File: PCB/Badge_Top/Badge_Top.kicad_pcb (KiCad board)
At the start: 2 copper layers, 65 x 75 mm, 34 parts

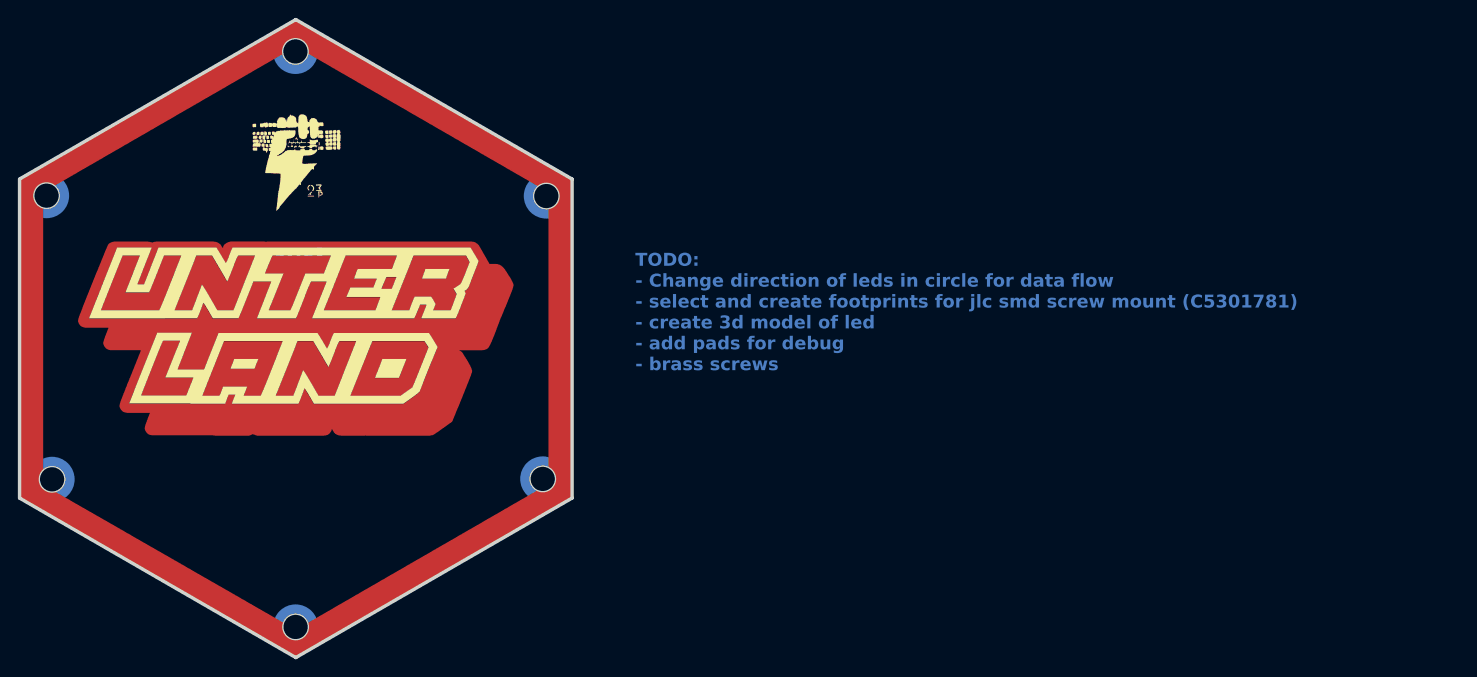
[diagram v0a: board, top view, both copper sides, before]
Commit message: do layout of top PCB, generated preliminary gerbers
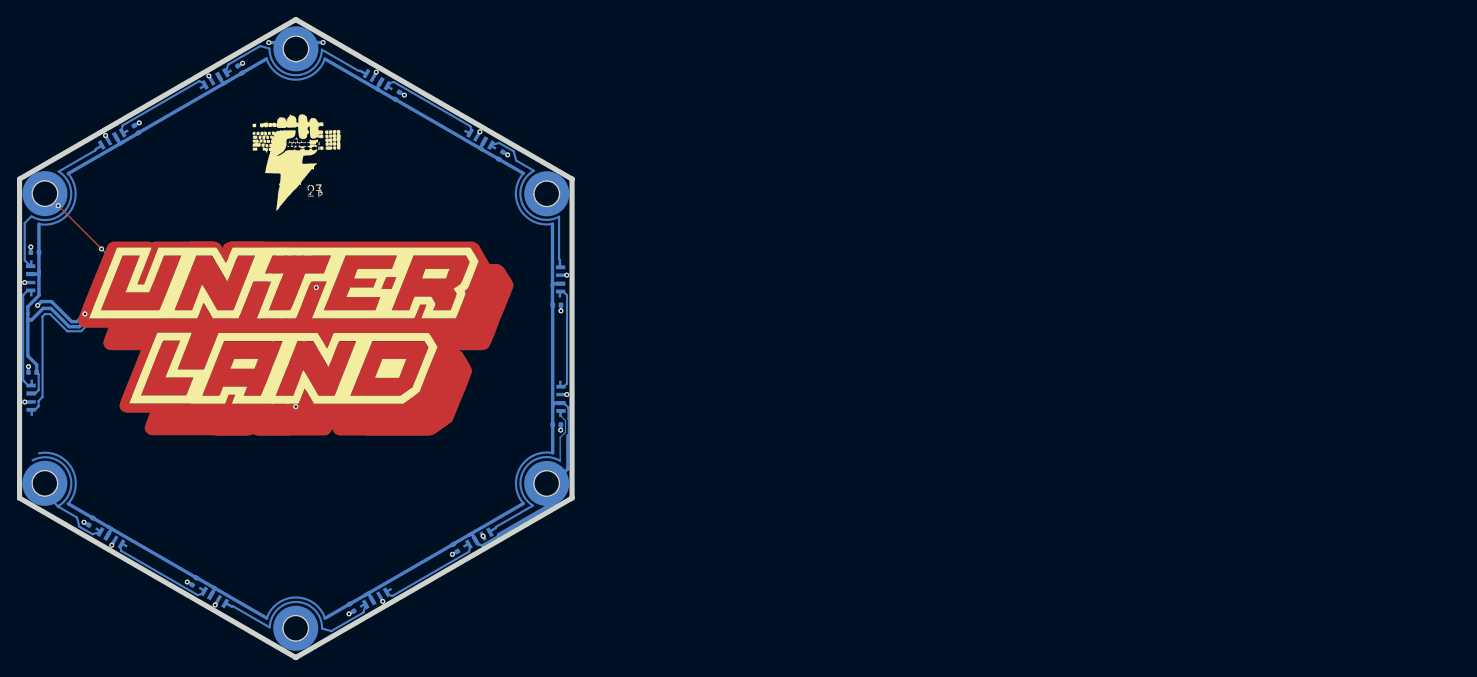
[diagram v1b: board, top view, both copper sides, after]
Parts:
- removed REF** (x6): Mounting_Wuerth_WA-SMSI-M2_H8mm_9774080243, Mounting_Wuerth:Mounting_Wuerth_WA-SMSI-M2_H8mm_9774080243
- added 1: , clipboard:9966cd8a-fa79-43c1-83f9-02636052551b, F.Cu at (143.6, 134.1)
- added 10: , clipboard:2488e693-1bf8-4f98-9257-4c9c6a257d6e, F.Cu at (137.1, 67.1)
- added 2: , clipboard:9966cd8a-fa79-43c1-83f9-02636052551b, F.Cu at (171.6, 114.4)
- added 3: , clipboard:9966cd8a-fa79-43c1-83f9-02636052551b, F.Cu at (168.5, 80.3)
- added 4: , clipboard:9966cd8a-fa79-43c1-83f9-02636052551b, F.Cu at (137.4, 65.9)
- added 5: , clipboard:9966cd8a-fa79-43c1-83f9-02636052551b, F.Cu at (109.4, 85.6)
- added 6: , clipboard:2488e693-1bf8-4f98-9257-4c9c6a257d6e, F.Cu at (113.7, 119.4)
- added 7: , clipboard:2488e693-1bf8-4f98-9257-4c9c6a257d6e, F.Cu at (143.9, 132.9)
- added 8: , clipboard:2488e693-1bf8-4f98-9257-4c9c6a257d6e, F.Cu at (170.7, 113.5)
- added 9: , clipboard:2488e693-1bf8-4f98-9257-4c9c6a257d6e, F.Cu at (167.3, 80.6)
- added ?: , clipboard:af2c86ee-64b2-4b61-864d-932c7bd539f4, F.Cu at (154.2, 105.8)
- added ?: , clipboard:2488e693-1bf8-4f98-9257-4c9c6a257d6e, F.Cu at (110.3, 86.5)
- added ?: , clipboard:9966cd8a-fa79-43c1-83f9-02636052551b, F.Cu at (112.5, 119.7)
- added J1: Conn_01x01, Mounting_Wuerth:Mounting_Wuerth_WA-SMSI-M2_H7mm_9774070243, B.Cu at (140.5, 65.9)
- added J2: Conn_01x01, Mounting_Wuerth:Mounting_Wuerth_WA-SMSI-M2_H7mm_9774070243, B.Cu at (111.0, 83.0)
- added J3: Conn_01x01, Mounting_Wuerth:Mounting_Wuerth_WA-SMSI-M2_H7mm_9774070243, B.Cu at (111.0, 117.0)
- added J4: Conn_01x01, Mounting_Wuerth:Mounting_Wuerth_WA-SMSI-M2_H7mm_9774070243, B.Cu at (140.5, 134.1)
- added J5: Conn_01x01, Mounting_Wuerth:Mounting_Wuerth_WA-SMSI-M2_H7mm_9774070243, B.Cu at (170.0, 117.0)
- added J6: Conn_01x01, Mounting_Wuerth:Mounting_Wuerth_WA-SMSI-M2_H7mm_9774070243, B.Cu at (170.0, 83.0)
- moved D10 10.4 mm to (171.7, 107.1), turned to -90 degrees
- moved D4 10.4 mm to (109.3, 92.9), turned to 90 degrees
- moved D6 10.4 mm to (131.0, 69.5), turned to 30 degrees
- moved D8 10.3 mm to (162.2, 76.5), turned to -30 degrees
- moved D14 10.3 mm to (118.8, 123.5), turned to 150 degrees
- moved D12 10.2 mm to (150.0, 130.5), turned to -150 degrees
- moved C6 9.96 mm to (133.9, 68.4), turned to 120 degrees
- moved C4 9.86 mm to (109.8, 89.9), turned to 180 degrees
- moved C10 9.80 mm to (171.2, 110.1), turned to 0 degrees
- moved C8 9.77 mm to (164.6, 78.5), turned to 60 degrees
- moved C12 9.77 mm to (147.1, 131.6), turned to -60 degrees
- moved C14 9.76 mm to (116.4, 121.5), turned to -120 degrees
- moved C5 7.07 mm to (121.8, 75.4)
- moved C3 7.06 mm to (109.5, 104.0)
- moved C7 7.02 mm to (152.4, 71.5)
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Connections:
- D1 pad 1: Net-(D1-DOUT) -> DOUT
- D1 pad 3: unconnected-(D1-DIN-Pad3) -> Net-(D1-DIN)
- D11 pad 1: Net-(D11-DOUT) -> Net-(D10-DIN)
- D11 pad 3: Net-(D10-DOUT) -> Net-(D11-DIN)
- D12 pad 1: Net-(D12-DOUT) -> Net-(D11-DIN)
- D12 pad 3: Net-(D11-DOUT) -> Net-(D12-DIN)
- D13 pad 1: unconnected-(D13-DOUT-Pad1) -> Net-(D12-DIN)
- D13 pad 3: Net-(D12-DOUT) -> Net-(D13-DIN)
- D14 pad 1: unconnected-(D14-DOUT-Pad1) -> Net-(D13-DIN)
- D14 pad 3: unconnected-(D14-DIN-Pad3) -> DIN
- D2 pad 1: Net-(D2-DOUT) -> Net-(D1-DIN)
- D2 pad 3: Net-(D1-DOUT) -> Net-(D2-DIN)
- D3 pad 1: Net-(D3-DOUT) -> Net-(D2-DIN)
- D3 pad 3: Net-(D2-DOUT) -> Net-(D3-DIN)
- D4 pad 1: Net-(D4-DOUT) -> Net-(D3-DIN)
- D4 pad 3: Net-(D3-DOUT) -> Net-(D4-DIN)
- D5 pad 1: Net-(D5-DOUT) -> Net-(D4-DIN)
- D5 pad 3: Net-(D4-DOUT) -> Net-(D5-DIN)
- D6 pad 1: Net-(D6-DOUT) -> Net-(D5-DIN)
- D6 pad 3: Net-(D5-DOUT) -> Net-(D6-DIN)
- D7 pad 1: Net-(D7-DOUT) -> Net-(D6-DIN)
- D7 pad 3: Net-(D6-DOUT) -> Net-(D7-DIN)
- D8 pad 1: Net-(D8-DOUT) -> Net-(D7-DIN)
- D8 pad 3: Net-(D7-DOUT) -> Net-(D8-DIN)
- D9 pad 1: Net-(D10-DIN) -> Net-(D8-DIN)
- D9 pad 3: Net-(D8-DOUT) -> Net-(D10-DOUT)
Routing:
- net VDD: track 0.00 -> 252.7 mm
- net Net-(D2-DIN): track 0.00 -> 56.5 mm
- net DOUT: track 0.00 -> 32.9 mm, vias 0 -> 2
- net GND: track 0.00 -> 31.8 mm, vias 0 -> 30
- net Net-(D1-DIN): track 0.00 -> 20.1 mm
- net Net-(D6-DIN): track 0.00 -> 12.5 mm
- net Net-(D12-DIN): track 0.00 -> 12.5 mm
- net Net-(D8-DIN): track 0.00 -> 12.5 mm
- net Net-(D4-DIN): track 0.00 -> 12.5 mm
- net Net-(D10-DIN): track 0.00 -> 12.4 mm
- net Net-(D3-DIN): track 0.00 -> 12.3 mm
- net Net-(D10-DOUT): track 0.00 -> 12.2 mm
- net Net-(D11-DIN): track 0.00 -> 12.2 mm
- net Net-(D5-DIN): track 0.00 -> 12.2 mm
- net Net-(D13-DIN): track 0.00 -> 12.2 mm
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- added copper zone on F.Cu, net GND
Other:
- outline, holes or cut-outs redrawn
- board text added: "TODO: - create 3d model of led - Outline to the edge? - Soldermask over round tracks around standoffs?"
- board text removed: "TODO: - Change direction of leds in circle for data flow - select and create footprints for jlc smd screw mount (C5301781) - create 3d model of led - add pads for debug - brass screws"

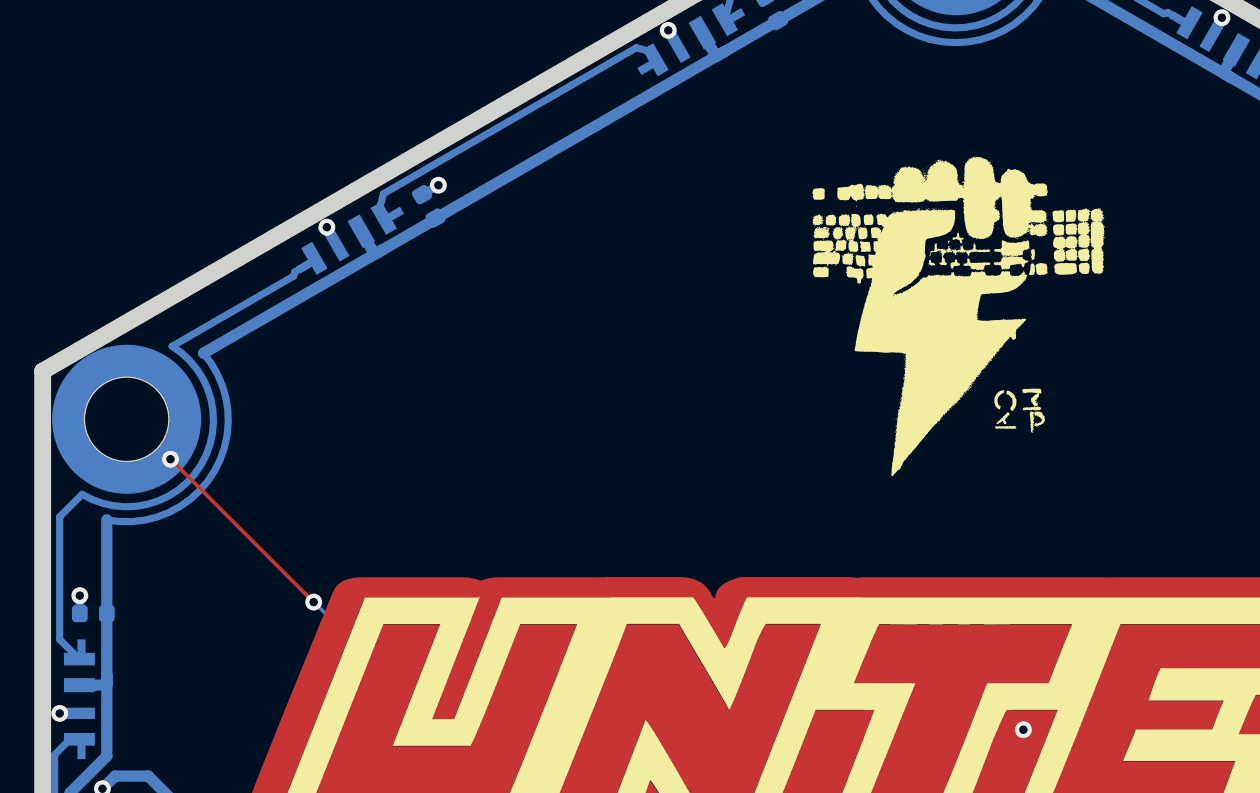
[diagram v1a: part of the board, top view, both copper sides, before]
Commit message: better silkscreen, remove DOUT
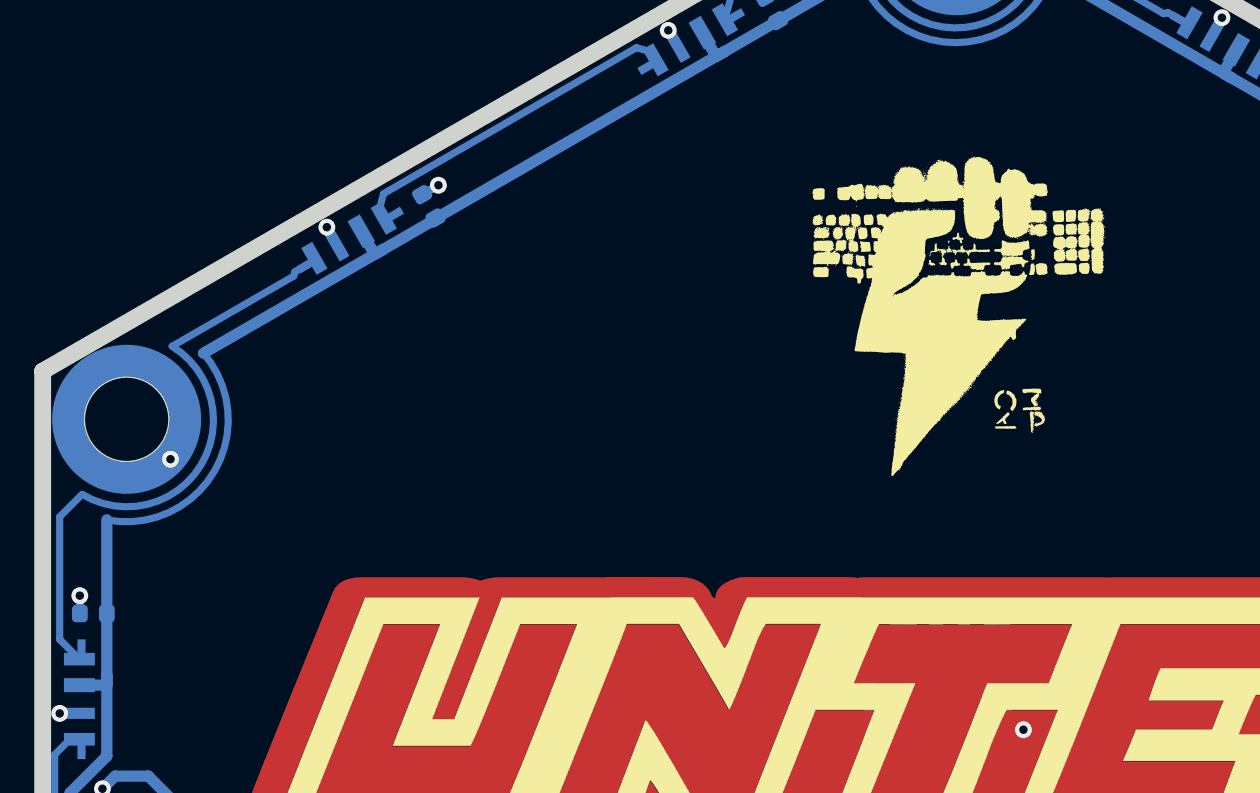
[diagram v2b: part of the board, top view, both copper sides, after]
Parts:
- added kibuzzard-64BC5FAA: G***, kibuzzard-64BC5FAA, B.Cu at (140.3, 97.4)
- added kibuzzard-64BC6378: G***, kibuzzard-64BC6378, B.Cu at (136.1, 66.7)
- added kibuzzard-64BC6382: G***, kibuzzard-64BC6382, B.Cu at (114.0, 120.4)
- added kibuzzard-64BC6413: G***, kibuzzard-64BC6413, B.Cu at (166.2, 120.8)
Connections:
- D1 pad 1: DOUT -> unconnected-(D1-DOUT-Pad1)
- J2 pad 1: DOUT -> unconnected-(J2-Pin_1-Pad1)
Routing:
- net DOUT: track 32.9 -> 0.00 mm, vias 2 -> 0
- net unconnected-(J2-Pin_1-Pad1): vias 0 -> 1
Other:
- board text added: "2023"
- board text added: "JLCJLCJLCJLC"
- board text added: "made with <3 by @crexodon @LeoDJ"

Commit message: finised pcb layout
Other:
- board text removed: "TODO: - create 3d model of led - Outline to the edge? - Soldermask over round tracks around standoffs?"
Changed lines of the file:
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@@
     (attr board_only exclude_from_pos_files exclude_from_bom)
     (fp_text reference "kibuzzard-64BC6378" (at 0 3.68681 30) (layer "B.SilkS") hide
-        (effects (font (size 0 0)) (justify mirror))
+        (effects (font (size 0 0) (thickness 0.15)) (justify mirror))
     )
     (fp_text value "G***" (at 0 -3.68681 30) (layer "B.SilkS") hide
-        (effects (font (size 0 0)) (justify mirror))
+        (effects (font (size 0 0) (thickness 0.15)) (justify mirror))
     )
     (fp_poly
@@
     (attr board_only exclude_from_pos_files exclude_from_bom)
     (fp_text reference "kibuzzard-64BC6413" (at 0 3.683 30) (layer "B.SilkS") hide
-        (effects (font (size 0 0)) (justify mirror))
+        (effects (font (size 0 0) (thickness 0.15)) (justify mirror))
     )
     (fp_text value "G***" (at 0 -3.683 30) (layer "B.SilkS") hide
-        (effects (font (size 0 0)) (justify mirror))
+        (effects (font (size 0 0) (thickness 0.15)) (justify mirror))
     )
     (fp_poly
@@
     (attr board_only exclude_from_pos_files exclude_from_bom)
     (fp_text reference "kibuzzard-64BC6382" (at 0 3.67284 330) (layer "B.SilkS") hide
-        (effects (font (size 0 0)) (justify mirror))
+        (effects (font (size 0 0) (thickness 0.15)) (justify mirror))
     )
     (fp_text value "G***" (at 0 -3.67284 330) (layer "B.SilkS") hide
-        (effects (font (size 0 0)) (justify mirror))
+        (effects (font (size 0 0) (thickness 0.15)) (justify mirror))
     )
     (fp_poly
@@
     (effects (font (size 1 1) (thickness 0.12)) (justify bottom mirror))
   )
-  (gr_text "TODO:\n- create 3d model of led\n- Outline to the edge?\n- Soldermask over round tracks around standoffs?" (at 180.4 103.9) (layer "Dwgs.User")
-    (effects (font (size 1.524 1.524) (thickness 0.3048) bold) (justify left bottom))
-  )
   (dimension (type aligned) (layer "Dwgs.User")
     (pts (xy 172.999818 81.25062) (xy 140.500001 62.499999))
     (height 6.214081)
-    (gr_text "37.5210 mm" (at 160.430013 65.49671 -29.98260097) (layer "Dwgs.User")
+    (gr_text "37,5210 mm" (at 160.430013 65.49671 -29.98260097) (layer "Dwgs.User")
       (effects (font (size 1 1) (thickness 0.15)))
     )
@@
     (pts (xy 172.999818 81.25062) (xy 156.737977 71.875))
     (height 2.95384)
-    (gr_text "18.7710 mm" (at 166.918659 73.007535 -29.96521561) (layer "Dwgs.User")
+    (gr_text "18,7710 mm" (at 166.918659 73.007535 -29.96521561) (layer "Dwgs.User")
       (effects (font (size 1 1) (thickness 0.15)))
     )
